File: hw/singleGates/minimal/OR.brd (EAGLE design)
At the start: 8 parts, among them Q1 BC817, Q2 BC817, Q3 BC817

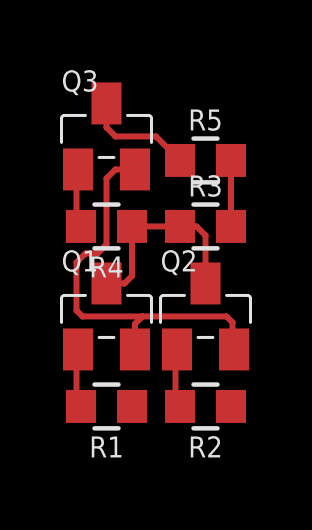
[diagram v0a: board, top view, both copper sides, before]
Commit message: Add led output and prepare first alu slice
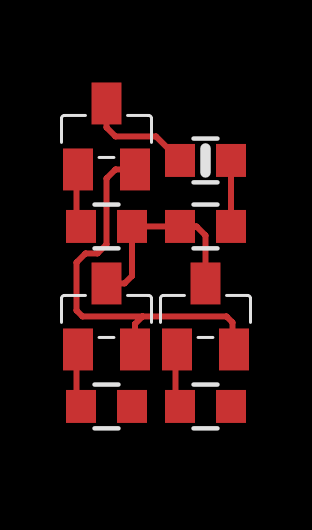
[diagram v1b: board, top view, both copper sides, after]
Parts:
- R5: device p.peter-gator:R0603 -> p.peter-rcl:R0603-MARK
